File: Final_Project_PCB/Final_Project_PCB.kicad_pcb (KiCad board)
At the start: 2 copper layers, 90 x 93 mm, 17 parts, among them J1 Screw_Terminal_01x03, J2 SR04 Sensor Jarak, J3 LDR, J4 Soil Moisture Sensor, K1 SRD-05VDC-SL-C, Q1 BC547, U1 ESP32-DEVKIT-V1, U2 DHT11

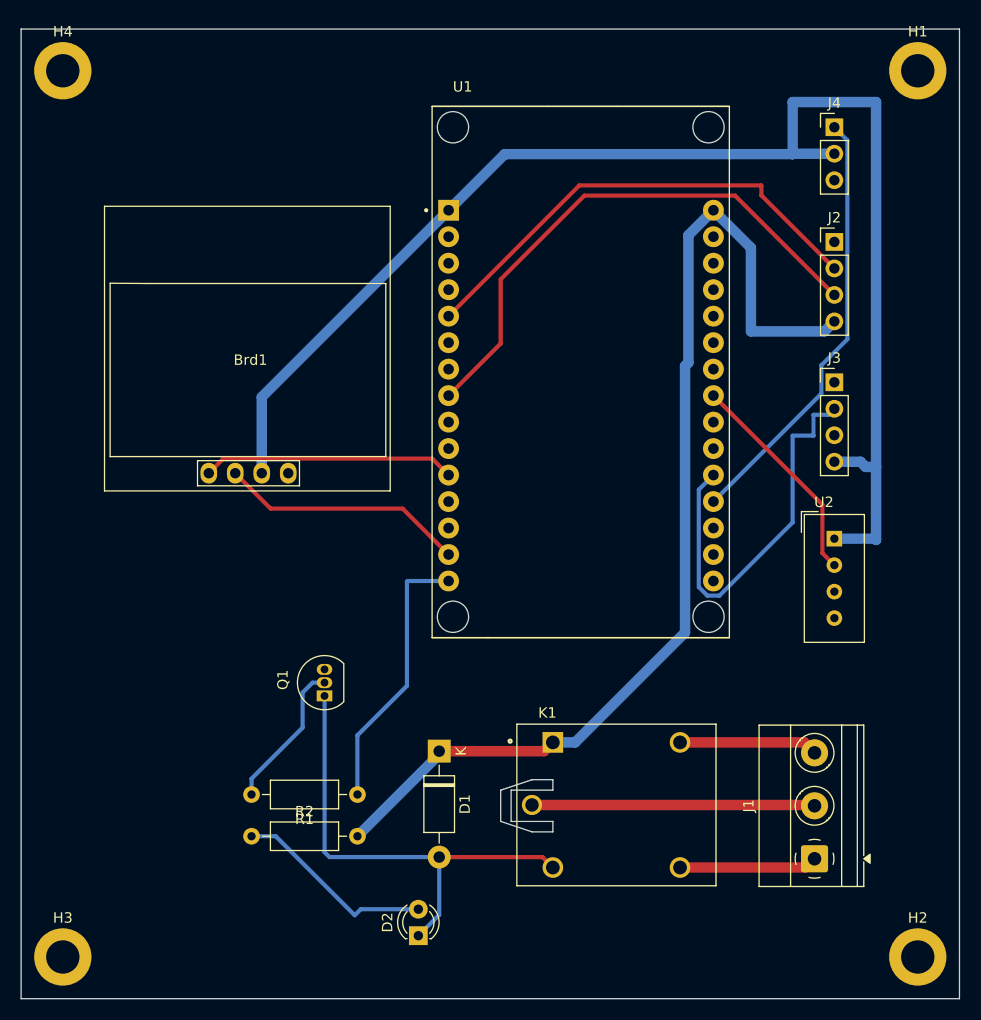
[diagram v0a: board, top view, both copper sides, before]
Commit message: adding ground layer
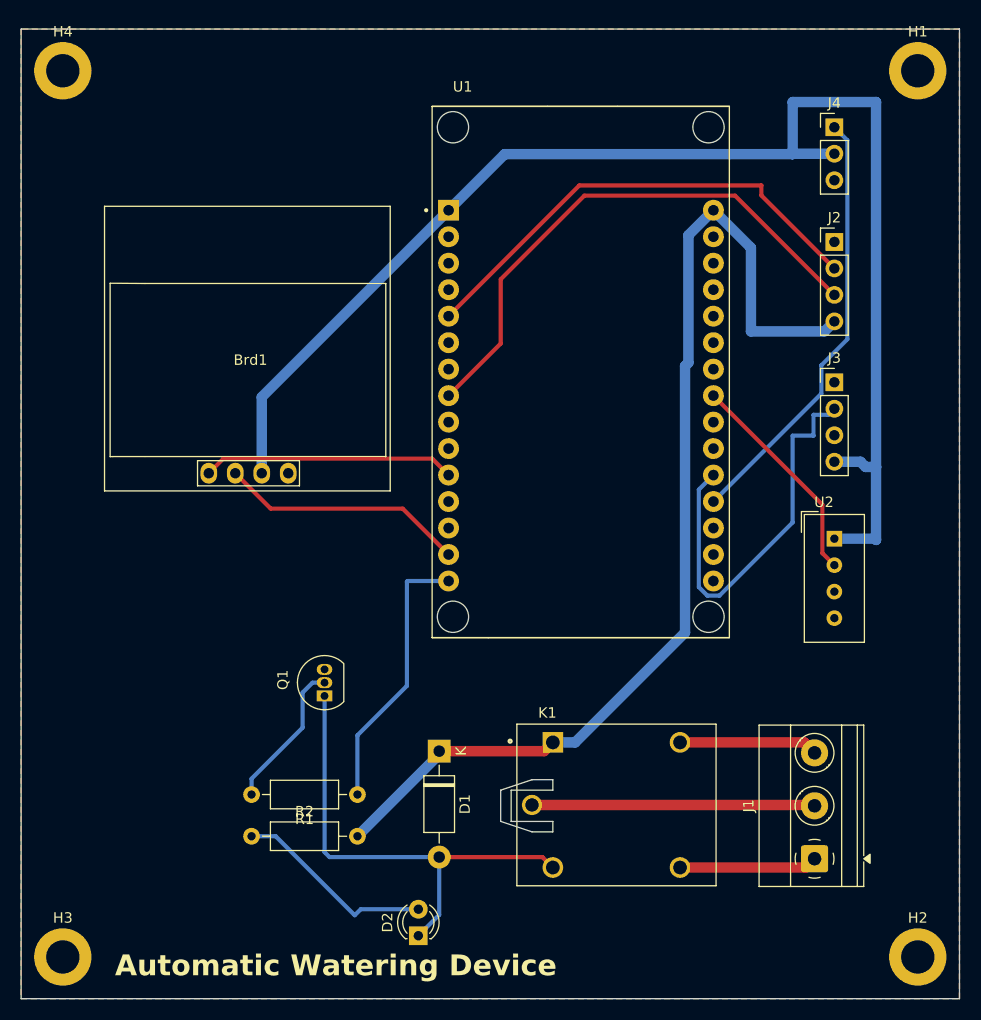
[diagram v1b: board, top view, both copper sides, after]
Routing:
- added copper zone on B.Cu, net GND
- added copper zone on F.Cu, net GND
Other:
- board text added: "Automatic Watering Device"
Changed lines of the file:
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@@
 		(layer "Edge.Cuts")
+	)
+	(gr_text "Automatic Watering Device"
+		(at 159 126 0)
+		(layer "F.SilkS")
+		(effects
+			(font
+				(size 2 2)
+				(thickness 0.4)
+				(bold yes)
+			)
+			(justify left bottom)
+		)
 	)
 	(segment
@@
 		(net 36)
 	)
+	(zone
+		(net 3)
+		(net_name "GND")
+		(layers "F.Cu" "B.Cu")
+		(hatch edge 0.5)
+		(connect_pads
+			(clearance 0.5)
+		)
+		(min_thickness 0.25)
+		(filled_areas_thickness no)
+		(fill yes
+			(thermal_gap 0.5)
+			(thermal_bridge_width 0.5)
+		)
+		(polygon
+			(pts
+				(xy 240 35) (xy 150 35) (xy 150 128) (xy 240 128)
+			)
+		)
+	)
 	(embedded_fonts no)
